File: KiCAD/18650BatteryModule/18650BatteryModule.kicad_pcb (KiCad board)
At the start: 2 copper layers, 94 x 70 mm, 17 parts, among them J1 DF1B-2S-2.5R, J2 DF11-8DP-2DS

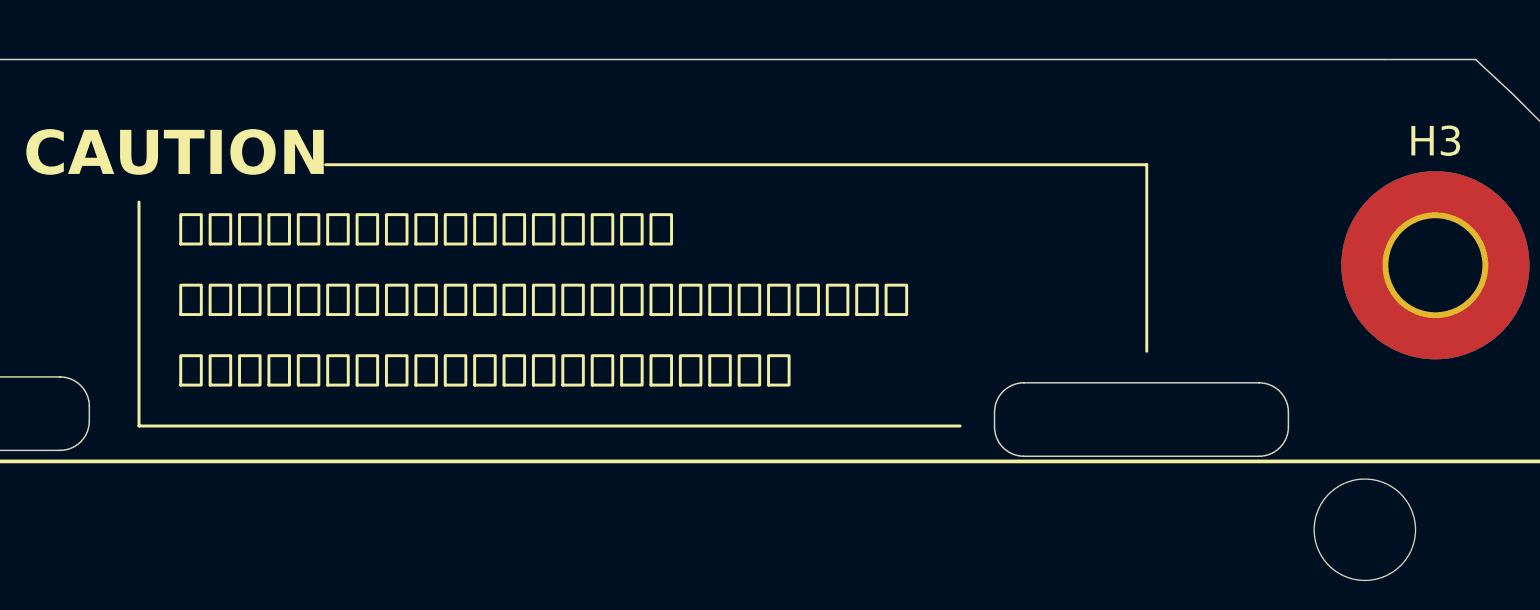
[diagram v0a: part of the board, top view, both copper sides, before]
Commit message: 何を修正したか忘れてしまった．
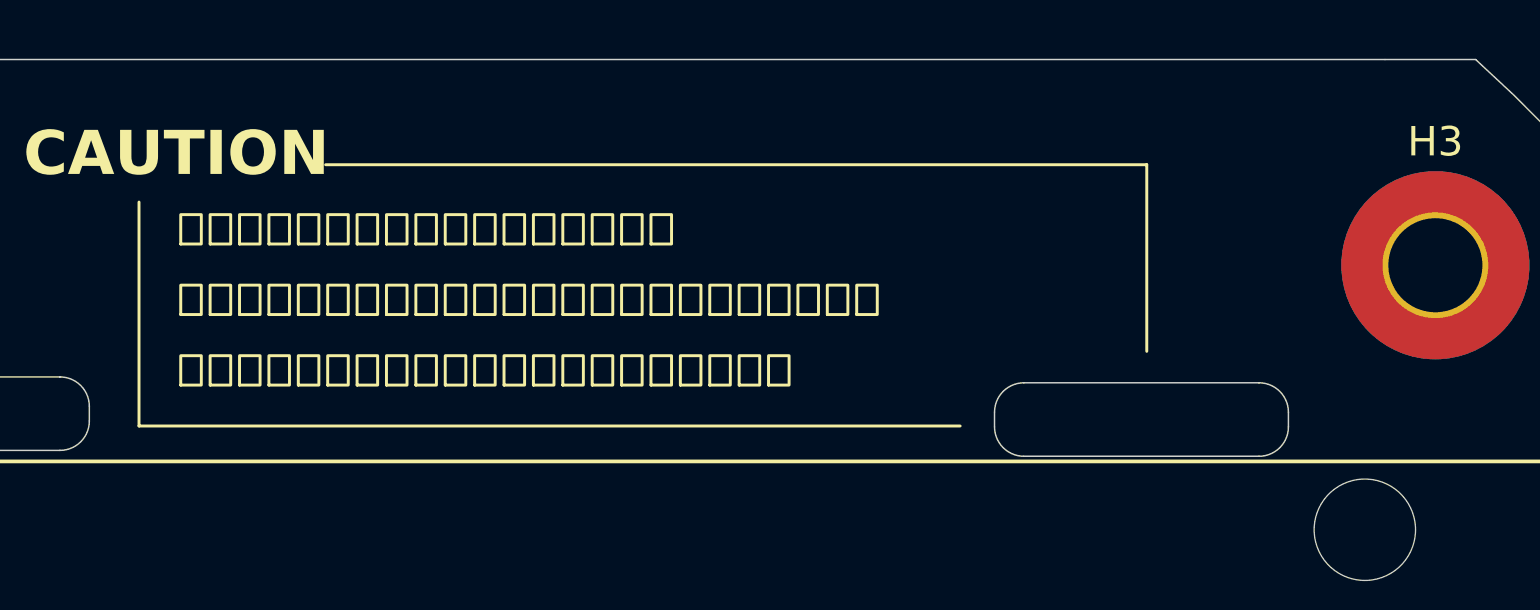
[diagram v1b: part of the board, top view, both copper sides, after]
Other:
- board text added: "運用する際，明確な対処法を決めてから使用すること"
- board text removed: "運用時する際，明確な対処法を決めてから使用すること"
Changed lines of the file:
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@@
 			(psnegative no)
 			(psa4output no)
-			(plot_black_and_white yes)
+			(plot_black_and_white no)
 			(sketchpadsonfab no)
 			(plotpadnumbers no)
@@
 			(crossoutdnponfab yes)
 			(subtractmaskfromsilk no)
-			(outputformat 1)
+			(outputformat 5)
 			(mirror no)
-			(drillshape 1)
+			(drillshape 2)
 			(scaleselection 1)
-			(outputdirectory "")
+			(outputdirectory "../../../../../Users/hirok/Downloads/A4ClearFile/18650BatteryModule/")
 		)
 	)
@@
 		(layer "Edge.Cuts")
 	)
-	(gr_text "運用時する際，明確な対処法を決めてから使用すること"
+	(gr_text "運用する際，明確な対処法を決めてから使用すること"
 		(at 137.16 73.8 0)
 		(layer "F.SilkS")
